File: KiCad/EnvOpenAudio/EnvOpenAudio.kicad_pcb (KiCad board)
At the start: 2 copper layers, 21 x 51 mm, 48 parts, among them J1 USB_C_Receptacle_USB2.0, J2 Button, J5 Conn_01x03_Male, U1 SOT-23-5 5.5V 3.3V 500mA, U3 RP2040, Y1 3225_4P 12MHz

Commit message: wired up audio IC
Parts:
- removed C102: 2.2uF 0402, Capacitor_SMD:C_0402_1005Metric
- removed C17, CBP1: 10uf 0402, Capacitor_SMD:C_0402_1005Metric
- removed NT1: NetTie_2, NetTie:NetTie-2_SMD_Pad0.5mm
- removed R10: 1 0402, Resistor_SMD:R_0402_1005Metric
- removed R101: 5.6K 0402, Resistor_SMD:R_0402_1005Metric
- removed R103: 10K 0402, Resistor_SMD:R_0402_1005Metric
- removed R9: 200 0603, Resistor_SMD:R_0603_1608Metric
- removed TP1, TP2, TP3: TestPoint, EnvExtras:CustomTestPoint
- added C12: 10uf 0402, Capacitor_SMD:C_0402_1005Metric, F.Cu at (63.3, 80.1)
- added C20: 10uf 0402, Capacitor_SMD:C_0402_1005Metric, F.Cu at (72.9, 74.4)
- added C21: 10uf 0402, Capacitor_SMD:C_0402_1005Metric, F.Cu at (72.5, 79.6)
- added C22: 0.1mF 0402, Capacitor_SMD:C_0402_1005Metric, F.Cu at (73.1, 84.2)
- added C23: 22mF 0402, Capacitor_SMD:C_0402_1005Metric, F.Cu at (72.1, 84.2)
- added C24: 0.1mF 0402, Capacitor_SMD:C_0402_1005Metric, F.Cu at (72.5, 81.5)
- added C25: 22mF 0402, Capacitor_SMD:C_0402_1005Metric, F.Cu at (71.5, 81.5)
- added C26: 0.1mF 0402, Capacitor_SMD:C_0402_1005Metric, F.Cu at (58.8, 82.8)
- added C27: 10mF 0402, Capacitor_SMD:C_0402_1005Metric, F.Cu at (59.8, 82.8)
- added C28: 0.1mF 0402, Capacitor_SMD:C_0402_1005Metric, F.Cu at (60.8, 81.9)
- added C29: 10mF 0402, Capacitor_SMD:C_0402_1005Metric, F.Cu at (61.8, 81.9)
- added C30: 0.1mF 0402, Capacitor_SMD:C_0402_1005Metric, F.Cu at (66.0, 78.6)
- added C31: 10mF 0402, Capacitor_SMD:C_0402_1005Metric, F.Cu at (66.8, 78.6)
- added C32: 0.1mF 0402, Capacitor_SMD:C_0402_1005Metric, F.Cu at (70.1, 86.4)
- added C33: 10mF 0402, Capacitor_SMD:C_0402_1005Metric, F.Cu at (71.1, 86.4)
- added C34: 47mF 0402, Capacitor_SMD:C_0402_1005Metric, F.Cu at (67.8, 78.6)
- added C35: 47mF 0402, Capacitor_SMD:C_0402_1005Metric, F.Cu at (65.0, 78.6)
- added C36: 1mF 0402, Capacitor_SMD:C_0402_1005Metric, F.Cu at (68.0, 90.7)
- added C37: 1mF 0402, Capacitor_SMD:C_0402_1005Metric, F.Cu at (67.0, 90.8)
- added C9: 10uf 0402, Capacitor_SMD:C_0402_1005Metric, F.Cu at (64.7, 74.9)
- added R12: 100K 0402, Resistor_SMD:R_0402_1005Metric, F.Cu at (71.0, 74.4)
- added R13: 22K 0402, Resistor_SMD:R_0402_1005Metric, F.Cu at (65.5, 90.3)
- added R8: 100K 0402, Resistor_SMD:R_0402_1005Metric, F.Cu at (62.8, 74.9)
- added U4: TLV320AIC3100, Package_DFN_QFN:VQFN-32-1EP_5x5mm_P0.5mm_EP3.5x3.5mm, F.Cu at (66.0, 84.0)
- added U5: TLV75518PDBV, Package_TO_SOT_SMD:SOT-23-5, F.Cu at (62.8, 77.5)
- added U6: TLV75533PDBV, Package_TO_SOT_SMD:SOT-23-5, F.Cu at (71.0, 77.0)
- D1: value 1N4002W -> schottky diode low forward voltage
- J2, RSW1: footprint Button_Switch_SMD:SW_Push_SPST_NO_Alps_SKRK -> Button_Switch_SMD:SW_SPST_B3U-1000P
- U1: value SOT-23-5 5.5V 3.3V 500mA -> TLV75533PDBV
- moved C16 55.4 mm to (60.9, 54.8), turned to 180 degrees
- moved C101 50.0 mm to (59.5, 36.5), turned to 0 degrees
- moved C13 48.7 mm to (71.8, 59.0), turned to 0 degrees
- moved R1 48.1 mm to (60.5, 50.1), turned to 180 degrees
- moved J5 47.8 mm to (68.9, 64.7), turned to 0 degrees
- moved RSW1 47.7 mm to (65.9, 71.7), turned to 0 degrees
- moved J2 47.6 mm to (61.8, 47.1), turned to 90 degrees
- moved R11 47.5 mm to (64.8, 66.0)
- moved C19 47.4 mm to (66.8, 66.0), turned to 180 degrees
- moved C10 47.2 mm to (69.0, 52.8)
- moved C7 47.2 mm to (64.8, 52.4), turned to 135 degrees
- moved FLASH1 47.2 mm to (61.6, 52.0)
- moved C3 47.0 mm to (68.0, 52.8)
- moved U3 46.9 mm to (66.0, 58.0)
- moved C5 46.8 mm to (64.0, 50.2), turned to 90 degrees
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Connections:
- C1 pad 1: Net-(U1-IN) -> VSYS
- D1 pad 1: VSYS -> Net-(D1-K)
- F1 pad 2: VSYS -> Net-(D1-K)
- FB1 pad 2: Net-(U1-IN) -> VSYS
- U1 pad 1: Net-(U1-IN) -> VSYS
- U1 pad 4: Net-(U1-BP) -> unconnected-(U1-NC-Pad4)
- U3 pad 2: /GPIO0 -> I2C0_SDA
- U3 pad 3: /GPIO1 -> I2C0_SCL
- U3 pad 4: /GPIO2 -> AUDIO_MCLK
- U3 pad 43: Net-(U3-ADC_AVDD) -> +3V3
- U3 pad 5: /GPIO3 -> AUDIO_BCLK
- U3 pad 6: /GPIO4 -> AUDIO_WCLK
- U3 pad 7: /GPIO5 -> AUDIO-DIN
- U3 pad 8: /GPIO6 -> AUDIO-DOUT
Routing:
- net VSYS: track 4.65 -> 72.2 mm, vias 0 -> 3
- net I2C0_SCL: track 0.00 -> 47.6 mm, vias 0 -> 2
- net I2C0_SDA: track 0.00 -> 45.3 mm
- net AUDIO_MCLK: track 0.00 -> 41.6 mm
- net AUDIO_BCLK: track 0.00 -> 40.3 mm
- net AUDIO_WCLK: track 0.00 -> 39.0 mm
- net AUDIO-DIN: track 0.00 -> 37.7 mm
- net AUDIO-DOUT: track 0.00 -> 36.5 mm
- net /GPIO24: track 30.6 -> 0.00 mm, vias 2 -> 0
- net +3V3: track 41.2 -> 61.6 mm, vias 3 -> 4
- net +1V8: track 0.00 -> 11.2 mm, vias 0 -> 2
- net MIC1RP: track 0.00 -> 9.66 mm, vias 0 -> 2
- net USB_D+: track 23.2 -> 14.3 mm, vias 1 -> 0
- net /SWCLK: track 12.3 -> 4.05 mm
- net /RUN: track 4.89 -> 12.6 mm
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- added copper zone on B.Cu, net +3V3
- removed copper zone on B.Cu, net AGND
- removed copper zone on F.Cu, net VBUS
- removed copper zone on F.Cu, net VSYS
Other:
- board size 21 x 51 mm -> 21.3 x 61.9 mm
- board text added: "BOOTSEL"
- board text added: "RESET"
- board text added: "SWCLK"
- board text added: "SWDIO"
- board text removed: "#REV 1.0"
- board text removed: "EnvOpenAudio"

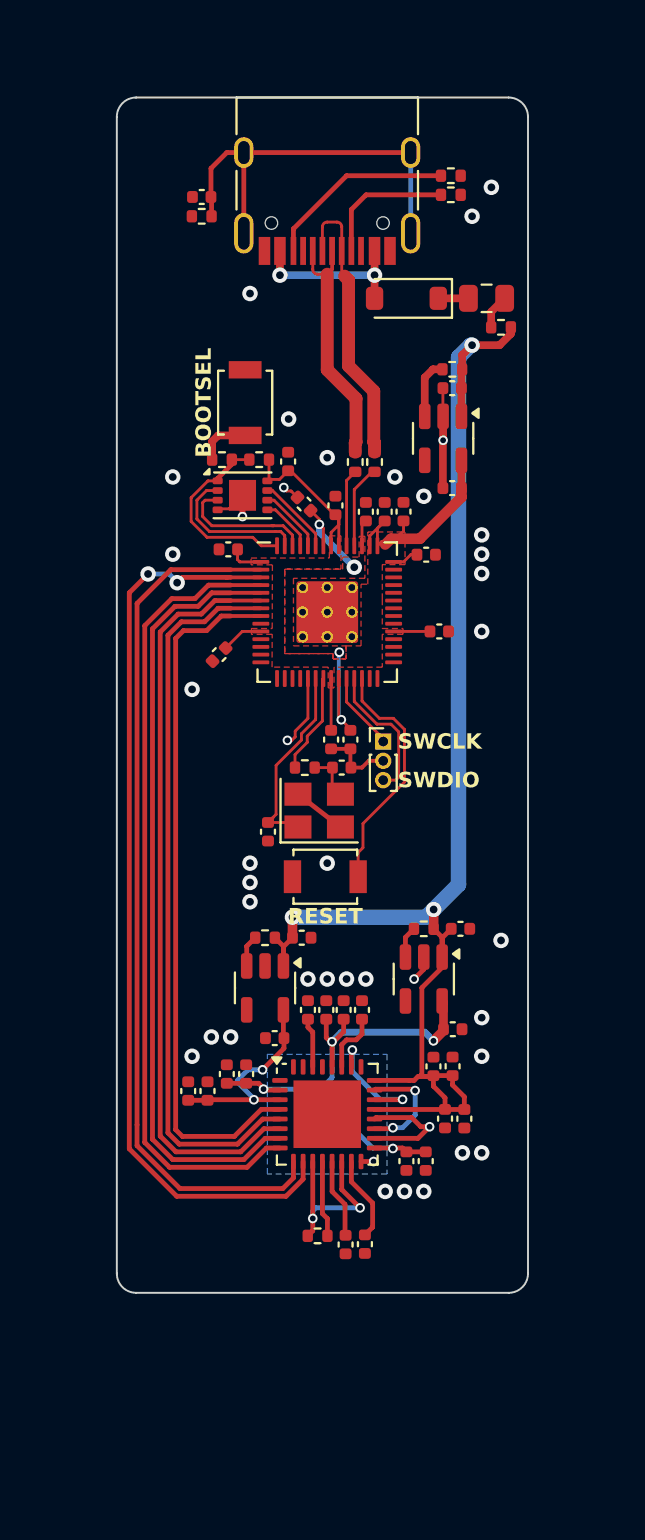
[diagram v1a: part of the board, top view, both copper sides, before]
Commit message: wired up majority of PCB, added headers and labels.
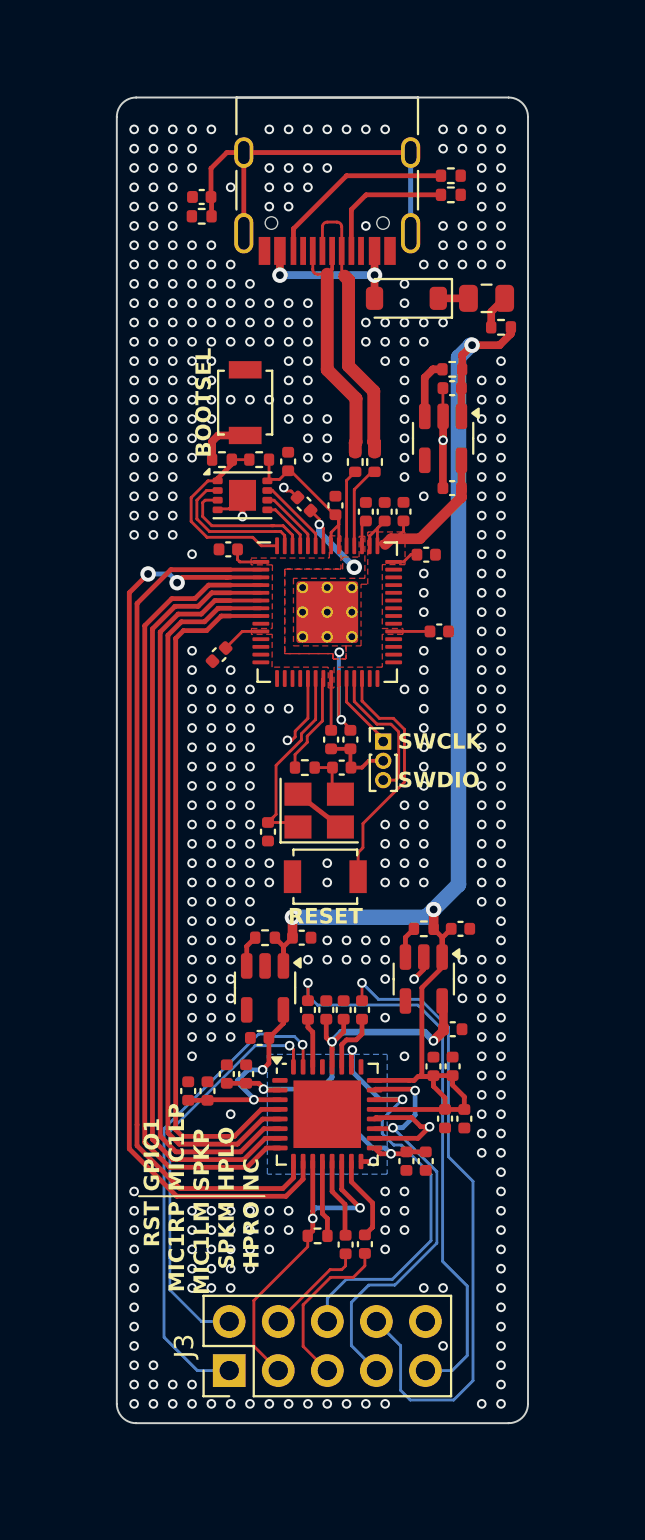
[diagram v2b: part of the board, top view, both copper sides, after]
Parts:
- added J3: Conn_01x10, Connector_PinHeader_2.54mm:PinHeader_2x05_P2.54mm_Vertical, F.Cu at (60.9, 97.3)
- moved C12 0.78 mm to (62.5, 80.0)
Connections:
- U4 pad 31: unconnected-(U4-~{RESET}-Pad31) -> AUDIO-RESET
- U4 pad 32: unconnected-(U4-GPIO1-Pad32) -> AUDIO-GPIO1
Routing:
- net HPLO: track 0.00 -> 33.6 mm, vias 0 -> 1
- net HPRO: track 0.00 -> 29.2 mm, vias 0 -> 1
- net AUDIO-RESET: track 0.00 -> 25.5 mm, vias 0 -> 1
- net AUDIO-GPIO1: track 0.00 -> 21.5 mm, vias 0 -> 1
- net SPKP: track 6.67 -> 23.5 mm
- net SPKM: track 5.81 -> 22.5 mm
- net MIC1RP: track 9.66 -> 18.3 mm
- net MIC1LM: track 0.00 -> 8.60 mm
- net MIC1LP: track 0.00 -> 5.30 mm
- net GND: vias 40 -> 480
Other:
- board size 21.3 x 61.9 mm -> 21.3 x 68.7 mm
- board text added: "GPIO1 MIC1LP SPKP HPLO NC"
- board text added: "RST MIC1RP MIC1LM SPKM HPRO"

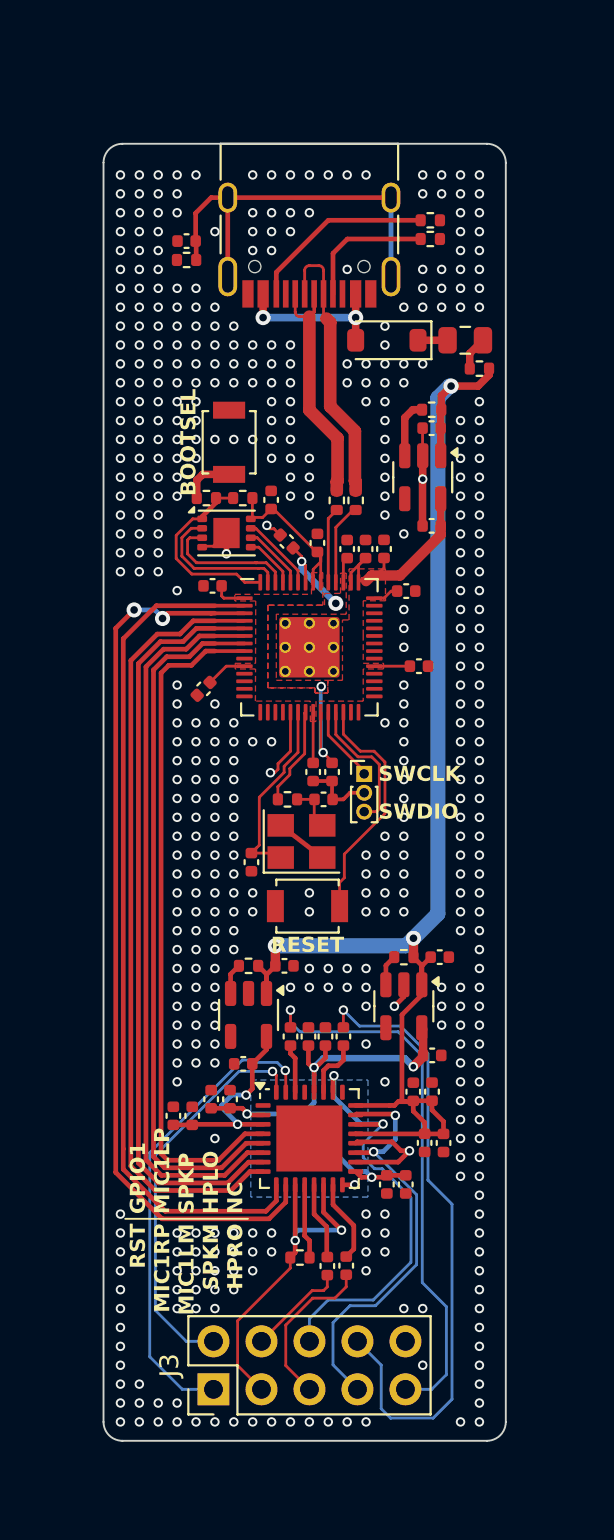
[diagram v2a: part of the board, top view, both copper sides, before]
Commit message: Swapped RP2040 for RP2350A for FPU, re-did board and schematic, added labels back and naming, Github link
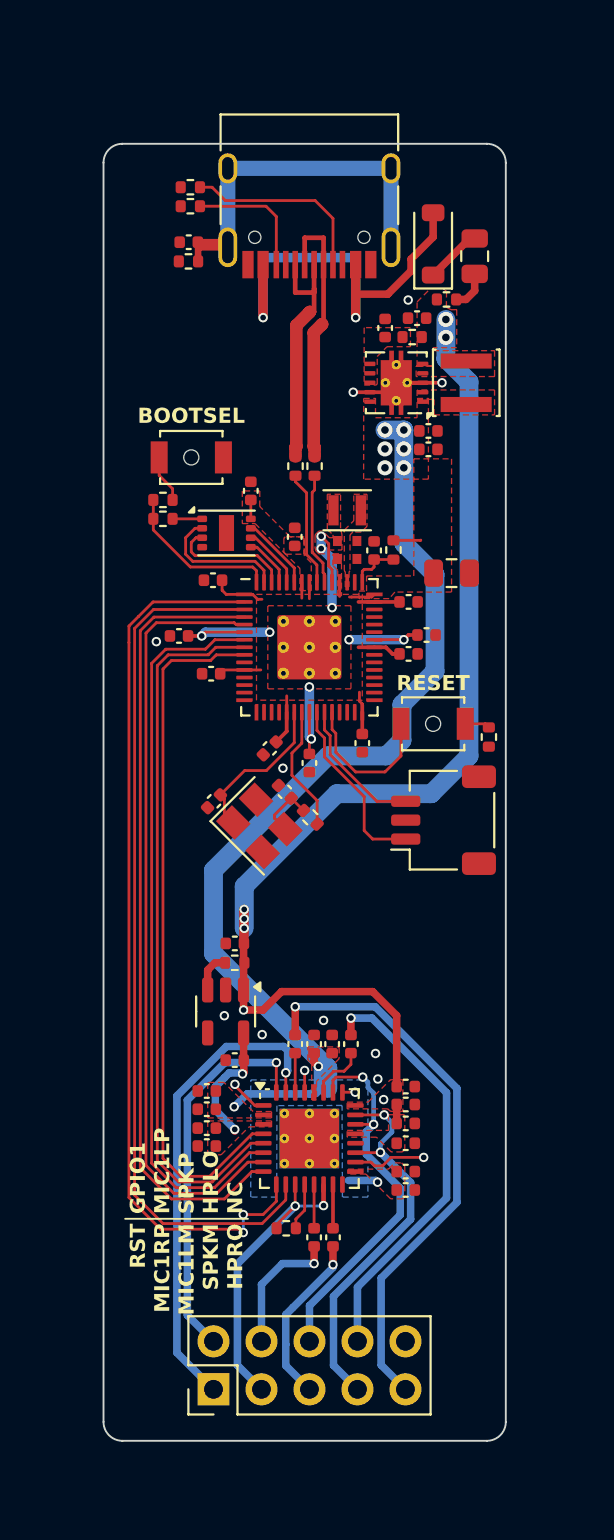
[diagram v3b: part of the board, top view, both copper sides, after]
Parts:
- removed C101: 0.1uf 0402, Capacitor_SMD:C_0402_1005Metric
- removed FLASH1: W25Q16JVUXIQ, Package_SON:SON-8-1EP_3x2mm_P0.5mm_EP1.4x1.6mm
- removed J5: Conn_01x03_Male, Connector_PinHeader_1.00mm:PinHeader_1x03_P1.00mm_Vertical
- removed R102: 220 0402, Resistor_SMD:R_0402_1005Metric
- removed R2: 10K 0402, Resistor_SMD:R_0402_1005Metric
- removed R6: 5.1K 0402, Resistor_SMD:R_0402_1005Metric
- removed RSW1: TSA343G00-250J2, Button_Switch_SMD:SW_SPST_B3U-1000P
- removed U6: TLV75533PDBV, Package_TO_SOT_SMD:SOT-23-5
- added C17: 100nf 0402, Capacitor_SMD:C_0402_1005Metric, F.Cu at (65.2, 52.2)
- added C38: 22mF 0402, Capacitor_SMD:C_0402_1005Metric, F.Cu at (71.1, 82.2)
- added C39: 1mF 0402, Capacitor_SMD:C_0402_1005Metric, F.Cu at (67.2, 89.2)
- added C40: 1mF 0402, Capacitor_SMD:C_0402_1005Metric, F.Cu at (66.2, 89.2)
- added L1: SPH3015H2R2MT, Inductor_SMD:L_Sunlord_SWPA3015S, F.Cu at (74.3, 44.0)
- added L2: 3.3uf 2016, Inductor_SMD:L_Murata_DFE201610P, F.Cu at (68.0, 50.8)
- added R10: 33r 0402, Resistor_SMD:R_0402_1005Metric, F.Cu at (70.5, 52.9)
- added R14: 27r 0402, Resistor_SMD:R_0402_1005Metric, F.Cu at (66.3, 48.4)
- added R15: 22K 0402, Resistor_SMD:R_0402_1005Metric, F.Cu at (64.8, 88.8)
- added R9: 1k 4020, Resistor_SMD:R_0402_1005Metric, F.Cu at (75.5, 62.8)
- added SW1: B3U-1000, Button_Switch_SMD:SW_SPST_B3U-1000P-B, F.Cu at (59.8, 48.0)
- added SW2: B3U-1000, Button_Switch_SMD:SW_SPST_B3U-1000P-B, F.Cu at (72.5, 62.0)
- added U2: TPS63001DRCR, Package_SON:Texas_DRC0010J_ThermalVias, F.Cu at (70.6, 44.0)
- C1: value 10uf 0402 -> 0.1uf 0402
- C10: value 2.2uF 0402 -> 10uF 0402
- C13, C14: value 100nf 0402 -> 4.7uf 0402
- C16: value 100nf 0402 -> 10uf 0402
- C19: value 22pf 0402 -> 100nf 0402
- C2: value 22pf 0402 -> 15pf 0402
- C20, C21, C4: value 10uf 0402 -> 100nf 0402
- C22: value 0.1mF 0402 -> 100nf 0402
- C23: value 22mF 0402 -> 100nf 0402
- C24: value 0.1mF 0402 -> 10uf 0805; footprint Capacitor_SMD:C_0402_1005Metric -> Capacitor_SMD:C_0805_2012Metric
- C25: value 22mF 0402 -> 0.1mF 0402
- C3: value 1uf 0402 -> 15pf 0402
- C32: value 0.1mF 0402 -> 10mF 0402
- C33: value 10mF 0402 -> 0.1mF 0402
- C34: value 47mF 0402 -> 0.1mF 0402
- C36: value 1mF 0402 -> 47mF 0402
- C37: value 1mF 0402 -> 22mF 0402
- C5: value 100nf 0402 -> 10uF 0402
- C6: value 100nf 0402 -> 0.1uF 0402
- C7, C8: value 100nf 0402 -> 4.7uf 0402; footprint Capacitor_SMD:C_0402_1005Metric -> RP2350_60QFN_minimal:C_0402_1005Metric_small_pads
- C9: value 10uf 0402 -> 10uF 0402
- J2: value Button -> SM03B-SRSS-TB; footprint Button_Switch_SMD:SW_SPST_B3U-1000P -> Connector_JST:JST_SH_SM03B-SRSS-TB_1x03-1MP_P1.00mm_Horizontal
- R1: value 1K 0402 -> 220 0402
- R11: value 1K 0402 -> 1k 4020
- R13: value 22K 0402 -> 27r 0402
- R3: value 27r 0402 resistor -> 0r 0402
- R4: value 27r 0402 resistor -> 5.1K 0402
- R7: value 100K 0402 -> 100ohm 0402
- R8: value 100K 0402 -> 1k 4020
- U1: value TLV75533PDBV -> W25Q16JVUXIQ; footprint Package_TO_SOT_SMD:SOT-23-5 -> Package_SON:SON-8-1EP_3x2mm_P0.5mm_EP1.4x1.6mm
- U3: value RP2040 -> TLV75518PDBV; footprint RP2040_minimal:RP2040-QFN-56 -> Package_TO_SOT_SMD:SOT-23-5
- U4: value TLV320AIC3100 -> RP2350_60QFN; footprint Package_DFN_QFN:VQFN-32-1EP_5x5mm_P0.5mm_EP3.5x3.5mm -> RP2350_60QFN_minimal:RP2350-QFN-60-1EP_7x7_P0.4mm_EP3.4x3.4mm_ThermalVias
- U5: value TLV75518PDBV -> TLV320AIC3100; footprint Package_TO_SOT_SMD:SOT-23-5 -> Package_DFN_QFN:VQFN-32-1EP_5x5mm_P0.5mm_EP3.15x3.15mm_ThermalVias
- Y1: value 3225_4P 12MHz -> ABM8-272-T3
- moved R13 41.9 mm to (65.3, 48.4), turned to -90 degrees
- moved C9 29.3 mm to (72.3, 46.5), turned to 0 degrees
- moved C23 28.6 mm to (71.2, 55.6), turned to 0 degrees
- moved C24 27.5 mm to (73.5, 54.1), turned to 0 degrees
- moved U4 26.0 mm to (66.0, 58.0)
- moved C22 26.0 mm to (71.2, 58.4), turned to 0 degrees
- moved C16 25.1 mm to (62.0, 79.8), turned to 0 degrees
- moved C6 23.7 mm to (70.0, 41.1), turned to 90 degrees
- moved J2 23.0 mm to (73.1, 67.2)
- moved U3 19.8 mm to (61.6, 77.3), turned to -90 degrees
- moved R4 18.7 mm to (59.7, 33.6), turned to 0 degrees
- moved R11 17.2 mm to (58.2, 50.2)
- moved C21 16.9 mm to (68.8, 63.1), turned to -90 degrees
- moved C1 16.2 mm to (59.6, 36.6), turned to 0 degrees
- moved C20 14.3 mm to (63.9, 63.4), turned to -135 degrees
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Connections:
- C1 pad 1: VSYS -> GND
- C1 pad 2: GND -> Net-(J1-SHIELD)
- C11 pad 1: +3V3 -> +1V1
- C12 pad 2: +1V8 -> VSYS
- C13 pad 1: +3V3 -> /VREG_AVDD
- C14 pad 1: +3V3 -> +1V1
- C15 pad 1: +3V3 -> +1V1
- C16 pad 1: +3V3 -> GND
- C16 pad 2: GND -> +1V8
- C19 pad 1: GND -> +3V3
- C19 pad 2: Net-(C19-Pad2) -> GND
- C2 pad 1: GND -> /XIN
- C2 pad 2: XIN -> GND
- C20 pad 1: GND -> +3V3
- C20 pad 2: VSYS -> GND
- C21 pad 1: GND -> +3V3
- C21 pad 2: +3V3 -> GND
- C22 pad 1: VSYS -> +3V3
- C23 pad 1: VSYS -> +3V3
- C24 pad 1: VSYS -> +3V3
- C25 pad 1: VSYS -> +3V3
- C27 pad 1: +1V8 -> +3V3
- C29 pad 1: +3V3 -> +1V8
- C3 pad 1: +1V1 -> Net-(C3-Pad1)
- C33 pad 1: +3V3 -> VSYS
- C34 pad 1: Net-(U4-HPL) -> VSYS
- C34 pad 2: HPLO -> GND
- C35 pad 1: Net-(U4-HPR) -> Net-(U5-HPL)
- C35 pad 2: HPRO -> HPLO
- C36 pad 1: Net-(U4-MIC1LM) -> Net-(U5-HPR)
- C36 pad 2: MIC1LM -> HPRO
- C37 pad 1: Net-(U4-MIC1LP) -> VSYS
- C37 pad 2: MIC1LP -> GND
- C5 pad 1: +3V3 -> VSYS
- C6 pad 1: +1V1 -> Net-(U2-EN)
- C7 pad 1: +1V1 -> +3V3
- C8 pad 1: +3V3 -> +1V1
- C9 pad 1: GND -> +3V3
- C9 pad 2: VSYS -> GND
- J2 pad 1: /~{USB_BOOT} -> /SWCLK
- R1 pad 1: /QSPI_SS -> Net-(J1-SHIELD)
- R1 pad 2: /~{USB_BOOT} -> GND
- R11 pad 1: XOUT -> /QSPI_SS
- R11 pad 2: Net-(C19-Pad2) -> /~{USB_BOOT}
- R12 pad 1: Net-(U6-EN) -> Net-(U3-EN)
- R13 pad 1: MIC1RP -> USB_D+
- R13 pad 2: Net-(U4-MICBIAS) -> Net-(U4-USB_DP)
- R3 pad 1: USB_D+ -> /QSPI_SS
- R3 pad 2: Net-(U3-USB_DP) -> /FLASH_SS
- R4 pad 1: USB_D- -> GND
- R4 pad 2: Net-(U3-USB_DM) -> Net-(J1-CC1)
- R5 pad 2: Net-(J1-CC1) -> Net-(J1-CC2)
- R7 pad 1: 3V3_EN -> VSYS
- R7 pad 2: VSYS -> Net-(U2-EN)
- R8 pad 1: Net-(U5-EN) -> /XOUT
- R8 pad 2: VSYS -> Net-(C3-Pad1)
- U1 pad 1: VSYS -> /FLASH_SS
- U1 pad 2: GND -> /QSPI_SD1
- U1 pad 3: 3V3_EN -> /QSPI_SD2
- U1 pad 4: unconnected-(U1-NC-Pad4) -> GND
- U1 pad 5: +3V3 -> /QSPI_SD0
- U3 pad 1: +3V3 -> VSYS
- U3 pad 2: I2C0_SDA -> GND
- U3 pad 3: I2C0_SCL -> Net-(U3-EN)
- U3 pad 4: AUDIO_MCLK -> unconnected-(U3-NC-Pad4)
- U3 pad 5: AUDIO_BCLK -> +1V8
- U4 pad 1: GND -> +3V3
- U4 pad 10: I2C0_SCL -> /GPIO7
- U4 pad 11: MIC1RP -> +3V3
- U4 pad 12: Net-(U4-MICBIAS) -> /GPIO8
- U4 pad 13: Net-(U4-MIC1LP) -> /GPIO9
- U4 pad 14: MIC1RP -> /GPIO10
- U4 pad 15: Net-(U4-MIC1LM) -> /GPIO11
- U4 pad 16: GND -> /GPIO12
- U4 pad 17: +3V3 -> /GPIO13
- U4 pad 18: GND -> /GPIO14
- U4 pad 19: SPKM -> /GPIO15
- U4 pad 2: +3V3 -> I2C0_SDA
- U4 pad 20: GND -> +3V3
- U4 pad 21: VSYS -> /XIN
- U4 pad 22: SPKP -> /XOUT
- U4 pad 23: SPKM -> +1V1
- U4 pad 24: VSYS -> /SWCLK
- U4 pad 25: GND -> /SWD
- U4 pad 26: SPKP -> /RUN
- U4 pad 27: Net-(U4-HPL) -> /GPIO16
- U4 pad 28: +3V3 -> /GPIO17
- U4 pad 29: GND -> /GPIO18
- U4 pad 3: +1V8 -> I2C0_SCL
- U4 pad 30: Net-(U4-HPR) -> +3V3
- U4 pad 31: AUDIO-RESET -> /GPIO19
- U4 pad 32: AUDIO-GPIO1 -> /GPIO20
- U4 pad 33: GND -> /GPIO21
- U4 pad 4: AUDIO-DOUT -> AUDIO_MCLK
- U4 pad 5: AUDIO-DIN -> AUDIO_BCLK
- U4 pad 6: AUDIO_WCLK -> +1V1
- U4 pad 7: AUDIO_BCLK -> AUDIO_WCLK
- U4 pad 8: AUDIO_MCLK -> AUDIO-DIN
- U4 pad 9: I2C0_SDA -> AUDIO-DOUT
- U5 pad 1: VSYS -> GND
- U5 pad 2: GND -> +3V3
- U5 pad 3: Net-(U5-EN) -> +1V8
- U5 pad 4: unconnected-(U5-NC-Pad4) -> AUDIO-DOUT
- U5 pad 5: +1V8 -> AUDIO-DIN
- Y1 pad 1: XIN -> /XIN
- Y1 pad 3: Net-(C19-Pad2) -> Net-(C3-Pad1)
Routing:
- net VBUS: track 8.61 -> 25.1 mm
- net GND: track 27.4 -> 13.1 mm, vias 480 -> 14
- net +3V3: track 61.7 -> 75.0 mm, vias 4 -> 9
- net VSYS: track 72.2 -> 59.7 mm, vias 3 -> 7
- net HPLO: track 33.6 -> 22.7 mm
- net +1V1: track 12.9 -> 23.8 mm, vias 4 -> 9
- net XIN: track 10.5 -> 0.00 mm
- net /XIN: track 0.00 -> 8.41 mm
- net /XOUT: track 0.00 -> 6.69 mm
- net Net-(U4-USB_DP): track 0.00 -> 6.11 mm
- net Net-(U4-USB_DM): track 0.00 -> 5.96 mm
- net /SWCLK: track 4.05 -> 9.68 mm
- net XOUT: track 5.22 -> 0.00 mm
- net /RUN: track 12.6 -> 8.13 mm
- net +1V8: track 11.2 -> 6.75 mm
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- added copper zone on F.Cu, net +1V8
- added copper zone on F.Cu, net /VREG_LX
- added copper zone on F.Cu, net Net-(U2-EN)
- added copper zone on F.Cu, net Net-(U2-L1)
- added copper zone on F.Cu, net Net-(U2-L2)
- added copper zone on F.Cu, net VSYS
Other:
- board text added: "EnvOpenAudio"
- board text added: "EnvOpenAudio V1.0 https://github.com/Envious-Data/EnvOpenAudio"
- board text added: "env"
- board text removed: "SWCLK"
- board text removed: "SWDIO"
